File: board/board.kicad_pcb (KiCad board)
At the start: 2 copper layers, 21 x 13 mm, 7 parts, among them J1 004_BASE-T_CT, J2 013_PoE_rectified

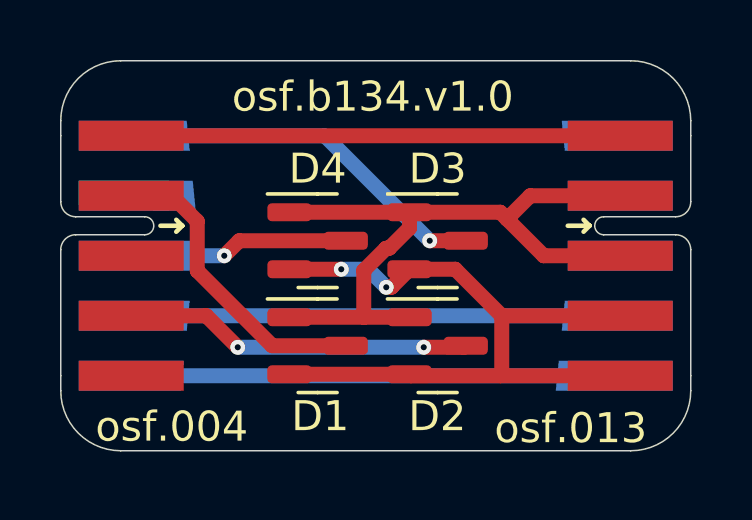
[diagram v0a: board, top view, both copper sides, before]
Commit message: fixed reverse polarity bug
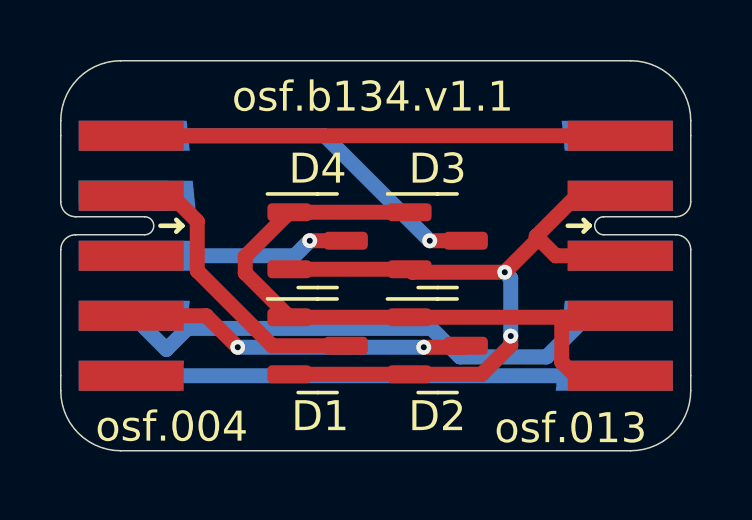
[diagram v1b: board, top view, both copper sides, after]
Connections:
- D1 pad 1: /rectifier/+ -> /rectifier/-
- D1 pad 2: /rectifier/- -> /rectifier/+
- D2 pad 1: /rectifier/+ -> /rectifier/-
- D2 pad 2: /rectifier/- -> /rectifier/+
- D3 pad 1: /rectifier/+ -> /rectifier/-
- D3 pad 2: /rectifier/- -> /rectifier/+
- D4 pad 1: /rectifier/+ -> /rectifier/-
- D4 pad 2: /rectifier/- -> /rectifier/+
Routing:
- net /rectifier/-: track 25.2 -> 23.4 mm, vias 2 -> 0
- net Net-(J1-3.3V): track 16.2 -> 17.9 mm
- net /rectifier/+: track 23.9 -> 25.6 mm, vias 0 -> 2
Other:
- board text added: "osf.b134.v1.1"
- board text removed: "osf.b134.v1.0"
